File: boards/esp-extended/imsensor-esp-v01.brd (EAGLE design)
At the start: 53.1 x 84.2 mm, 42 parts, among them J1-A2 PJ-313-SPAD, J2-A3 PJ-313-SPAD, J3-A4 PJ-313-SPAD, J4-A5 PJ-313-SPAD, J5-D9 PJ-313-SPAD, J6-D6 PJ-313-SPAD, J7-D5 PJ-313-SPAD, J8-D3 PJ-313-SPAD, Q1 MOSFET-NCHANNEL2N7000, Q2 MOSFET-NCHANNEL2N7000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

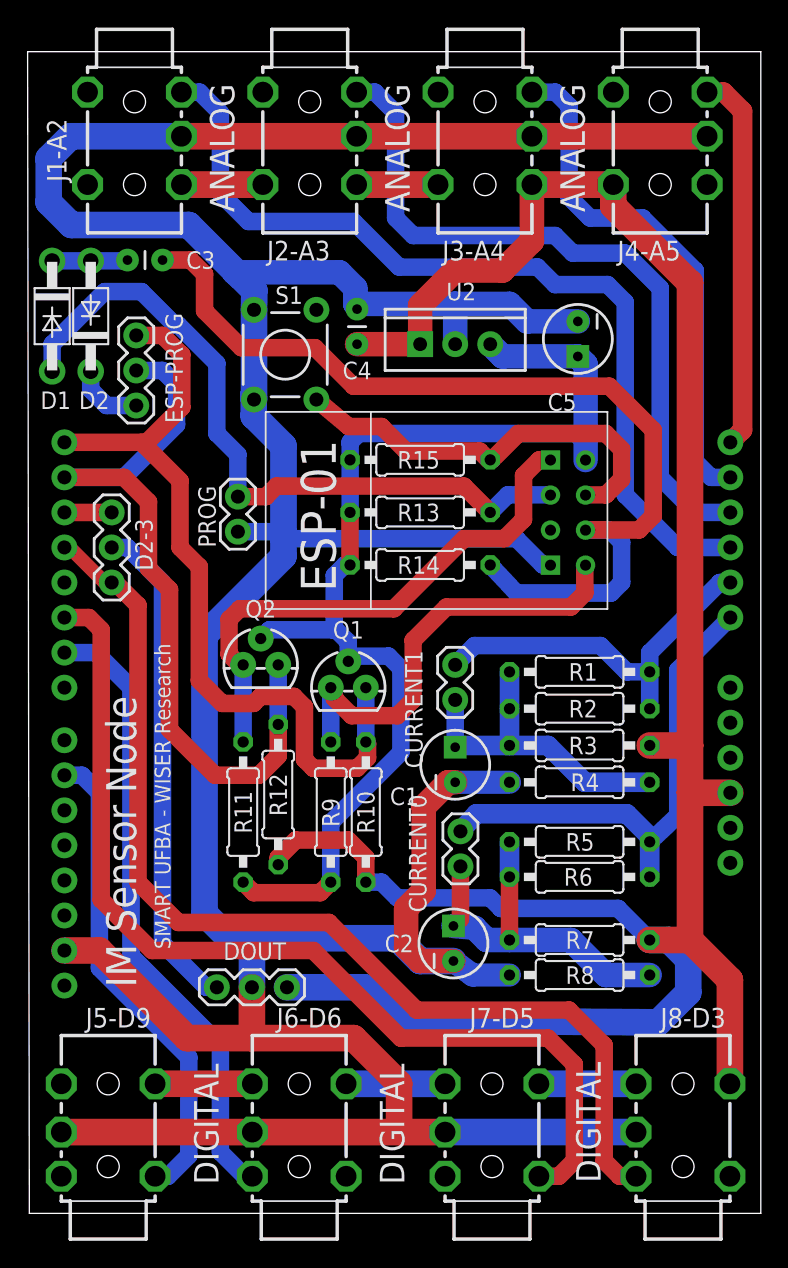
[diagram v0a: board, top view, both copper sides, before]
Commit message: Cleaned and organized IMSensor for ESP8266 V1
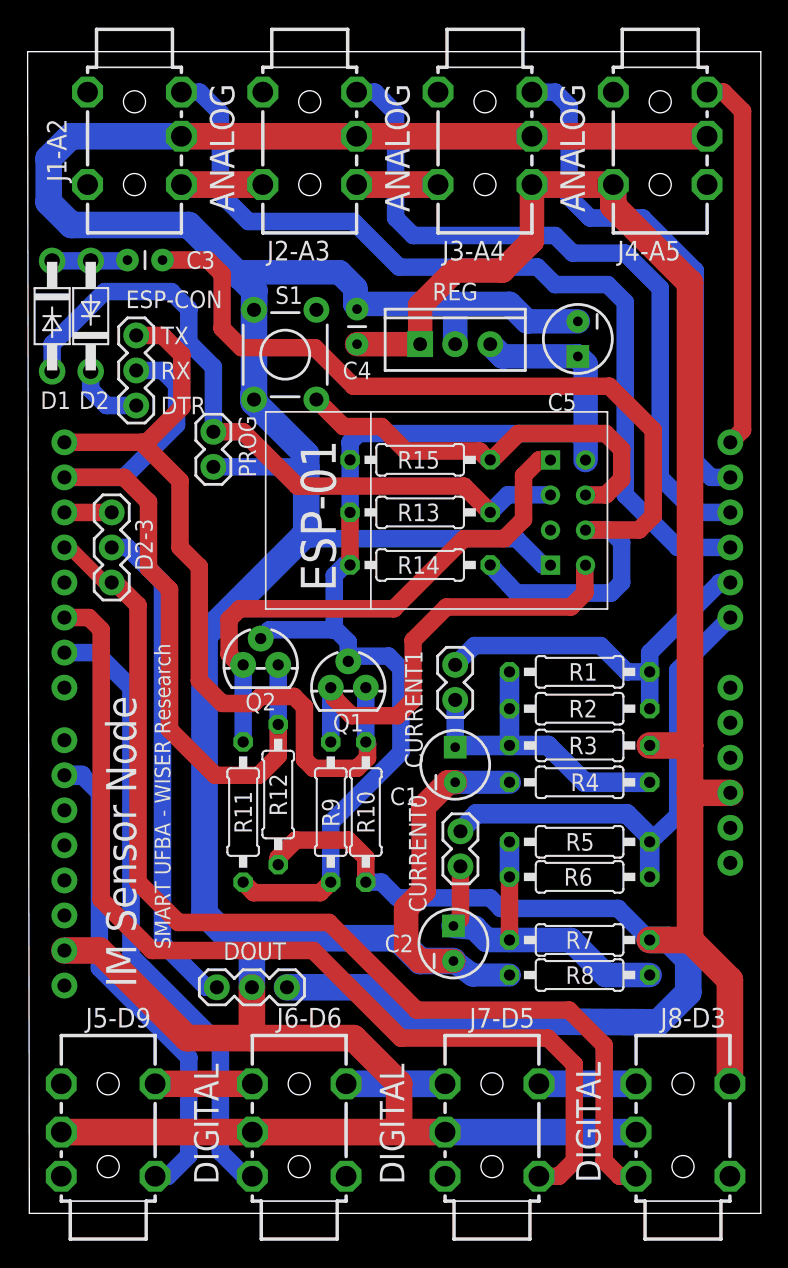
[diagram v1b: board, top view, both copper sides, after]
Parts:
- C5: value 10uF -> 47uF
- moved PROG 5.02 mm to (13.3, 56.6)
- renumbered ESP-PROG to ESP-CON, U2 to REG
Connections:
- net DEK renamed A0
- net J5 renamed D6
- net N$10 renamed A1
- net N$11 renamed BURDEN-C1
- net N$12 renamed D9
- net N$13 renamed D3
- net N$15 renamed A5
- net N$17 renamed BURDEN-C0
- net N$18 renamed ESP-TX
- net N$20 renamed RST
- net N$21 renamed ESP-RX
- net N$22 renamed CH-PD
- net N$25 renamed GPIO0
- net N$3 renamed A4
- net N$4 renamed A3
- net N$5 renamed A2
- net N$6 renamed D5
- net RX renamed UC-TX
- net TX renamed UC-RX
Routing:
- net GND: track 301.6 -> 304.9 mm
- net GPIO0: track 52.2 -> 51.0 mm
- net CH-PD: track 70.4 -> 71.1 mm
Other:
- board text added: "DTR"
- board text added: "RX"
- board text added: "TX"
